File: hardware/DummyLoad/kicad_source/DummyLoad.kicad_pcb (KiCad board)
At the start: 2 copper layers, 34 x 40 mm, 55 parts, among them CN1 CON-SMA-EDGE-S-ND, CN2 CON-SMA-EDGE-S-ND

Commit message: added pdf files, licence files, gerber files. updated data for release, generated zip file
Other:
- board text added: "Copyright generationmake 2018 see full project documentation at http://ardutrx.generationmake.de This documentation describes Open Hardware and is licensed under the CERN OHL v. 1.2. You may redistribute and modify this documentation under the terms of the CERN OHL v.1.2. (http://ohwr.org/cernohl). This documentation is distributed WITHOUT ANY EXPRESS OR IMPLIED WARRANTY, INCLUDING OF MERCHANTABI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"
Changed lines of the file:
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@@
   (general
     (thickness 1.6)
-    (drawings 20)
+    (drawings 21)
     (tracks 197)
     (zones 0)
@@
   )
   (page A4)
+  (title_block
+    (title "ArduTrx Dummy Load")
+    (date 2019-05-30)
+    (rev 1.0)
+    (company generationmake)
+  )
   (layers
     (0 F.Cu signal)
@@
     (pcbplotparams
       (layerselection 0x010fc_ffffffff)
-      (usegerberextensions false)
+      (usegerberextensions true)
       (usegerberattributes false)
       (usegerberadvancedattributes false)
@@
       (outputformat 1)
       (mirror false)
-      (drillshape 1)
+      (drillshape 0)
       (scaleselection 1)
-      (outputdirectory ""))
+      (outputdirectory "../gerber"))
   )
   (net 0 "")
@@
       (xy 5.541591 2.802653)) (layer B.SilkS) (width 0.01))
   )
+  (gr_text "Copyright generationmake 2018\nsee full project documentation at http://ardutrx.generationmake.de\n\nThis   documentation   describes   Open   Hardware   and   is   licensed   \nunder   the CERN OHL v. 1.2.\nYou may redistribute and modify this documentation under the terms \nof the CERN OHL v.1.2. (http://ohwr.org/cernohl). This documentation \nis distributed WITHOUT   ANY   EXPRESS   OR   IMPLIED   WARRANTY, \nINCLUDING   OF MERCHANTABILITY,   SATISFACTORY   QUALITY   AND \nFITNESS   FOR   A PARTICULAR   PURPOSE.   Please   see   the   CERN   \nOHL   v.1.2  for   applicable conditions" (at 179.2 145.85) (layer Cmts.User)
+    (effects (font (size 1.5 1.5) (thickness 0.3)) (justify left))
+  )
   (gr_text "Licensed under \nCERN OHL v 1.2" (at 87.5 113.5 90) (layer B.SilkS)

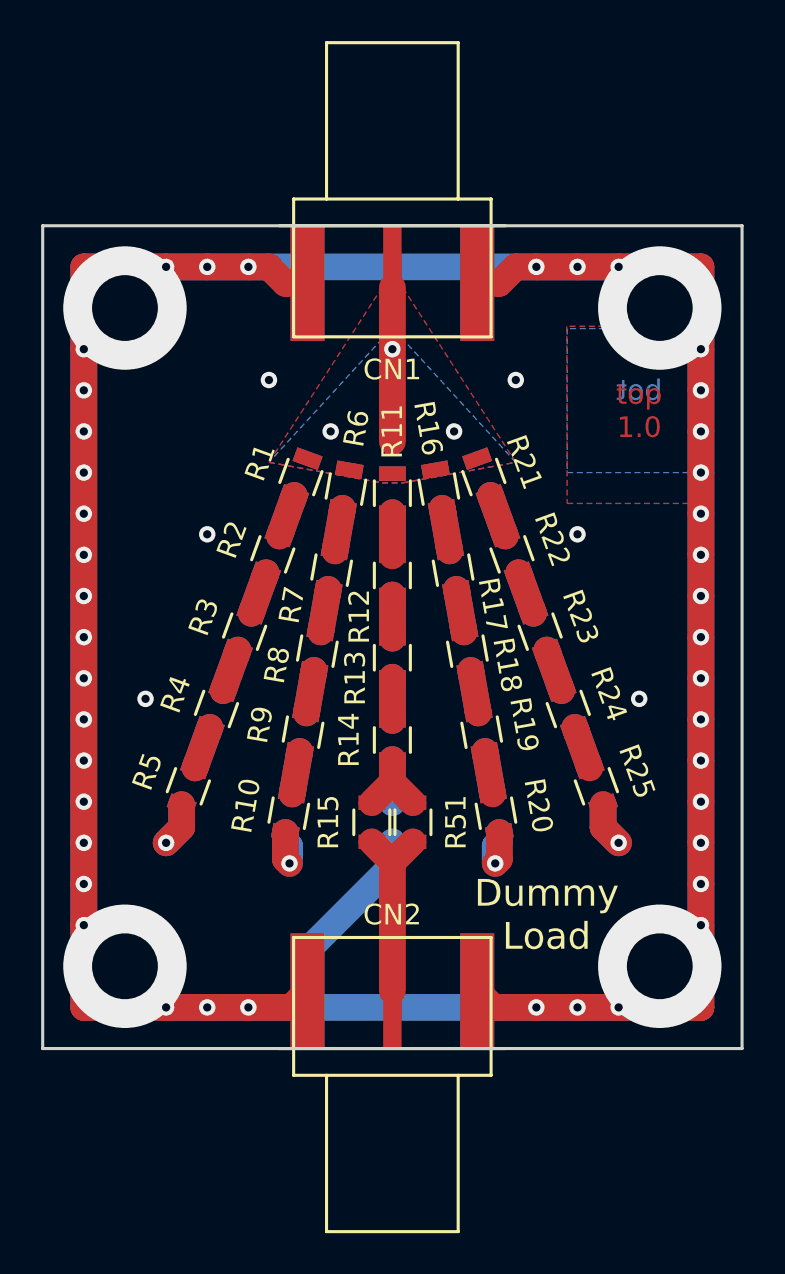
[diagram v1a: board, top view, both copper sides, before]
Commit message: reworked schematic to have 50 ohms on input and output
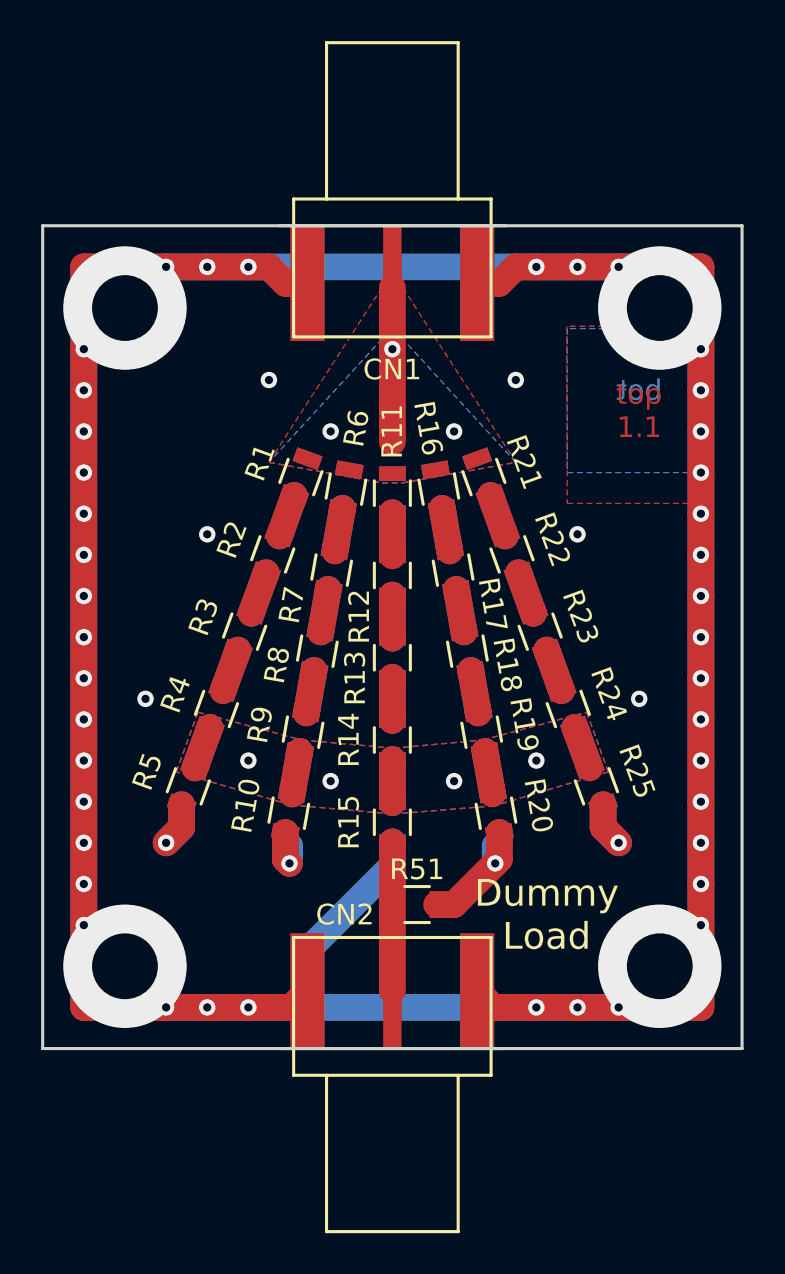
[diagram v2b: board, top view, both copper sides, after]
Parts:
- removed the G*** at (100.0, 135.5)
- R15: value 100R -> 62R
- R51: value 100R -> 160R
- moved R51 4.00 mm to (101.2, 133.0), turned to 0 degrees
- moved R15 1.00 mm to (100.0, 129.0)
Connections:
- R14 pad 2: Net-(R14-Pad2) -> Net-(R10-Pad1)
- R15 pad 1: Net-(R14-Pad2) -> Net-(R10-Pad1)
- R19 pad 2: Net-(R19-Pad2) -> Net-(R10-Pad1)
- R20 pad 1: Net-(R19-Pad2) -> Net-(R10-Pad1)
- R24 pad 2: Net-(R24-Pad2) -> Net-(R10-Pad1)
- R25 pad 1: Net-(R24-Pad2) -> Net-(R10-Pad1)
- R29 pad 2: Net-(R29-Pad2) -> Net-(R10-Pad1)
- R30 pad 1: Net-(R29-Pad2) -> Net-(R10-Pad1)
- R34 pad 2: Net-(R34-Pad2) -> Net-(R10-Pad1)
- R35 pad 1: Net-(R34-Pad2) -> Net-(R10-Pad1)
- R39 pad 2: Net-(R39-Pad2) -> Net-(R10-Pad1)
- R4 pad 2: Net-(R4-Pad2) -> Net-(R10-Pad1)
- R40 pad 1: Net-(R39-Pad2) -> Net-(R10-Pad1)
- R44 pad 2: Net-(R44-Pad2) -> Net-(R10-Pad1)
- R45 pad 1: Net-(R44-Pad2) -> Net-(R10-Pad1)
- R49 pad 2: Net-(R49-Pad2) -> Net-(R10-Pad1)
- R5 pad 1: Net-(R4-Pad2) -> Net-(R10-Pad1)
- R50 pad 1: Net-(R49-Pad2) -> Net-(R10-Pad1)
- R51 pad 1: Net-(R14-Pad2) -> /HF_OUT
- R51 pad 2: /HF_OUT -> GND
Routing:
- net Net-(R10-Pad1): track 2.10 -> 20.9 mm, vias 0 -> 4
- net Net-(R14-Pad2): track 3.93 -> 0.00 mm
- net GND: track 272.8 -> 276.5 mm
- net Net-(R44-Pad2): track 2.10 -> 0.00 mm
- net Net-(R19-Pad2): track 2.10 -> 0.00 mm
- net Net-(R49-Pad2): track 2.10 -> 0.00 mm
- net Net-(R4-Pad2): track 2.10 -> 0.00 mm
- net Net-(R24-Pad2): track 2.10 -> 0.00 mm
- net Net-(R39-Pad2): track 2.10 -> 0.00 mm
- net Net-(R34-Pad2): track 2.05 -> 0.00 mm
- net Net-(R29-Pad2): track 2.05 -> 0.00 mm
- net /HF_OUT: track 9.08 -> 7.25 mm
- added copper zone on B.Cu, net Net-(R10-Pad1)
- added copper zone on F.Cu, net Net-(R10-Pad1)
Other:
- board text added: "Copyright generationmake 2019 see full project documentation at http://ardutrx.generationmake.de This documentation describes Open Hardware and is licensed under the CERN OHL v. 1.2. You may redistribute and modify this documentation under the terms of the CERN OHL v.1.2. (http://ohwr.org/cernohl). This documentation is distributed WITHOUT ANY EXPRESS OR IMPLIED WARRANTY, INCLUDING OF MERCHANTABI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"
- board text added: "top 1.1"
- board text removed: "Copyright generationmake 2018 see full project documentation at http://ardutrx.generationmake.de This documentation describes Open Hardware and is licensed under the CERN OHL v. 1.2. You may redistribute and modify this documentation under the terms of the CERN OHL v.1.2. (http://ohwr.org/cernohl). This documentation is distributed WITHOUT ANY EXPRESS OR IMPLIED WARRANTY, INCLUDING OF MERCHANTABI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"
- board text removed: "top 1.0"
